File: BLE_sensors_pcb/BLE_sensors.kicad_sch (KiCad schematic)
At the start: 16 parts, among them J2 Conn_01x02, J3 USB_C_Receptacle, U1 BME280, U2 LSM303AHTR

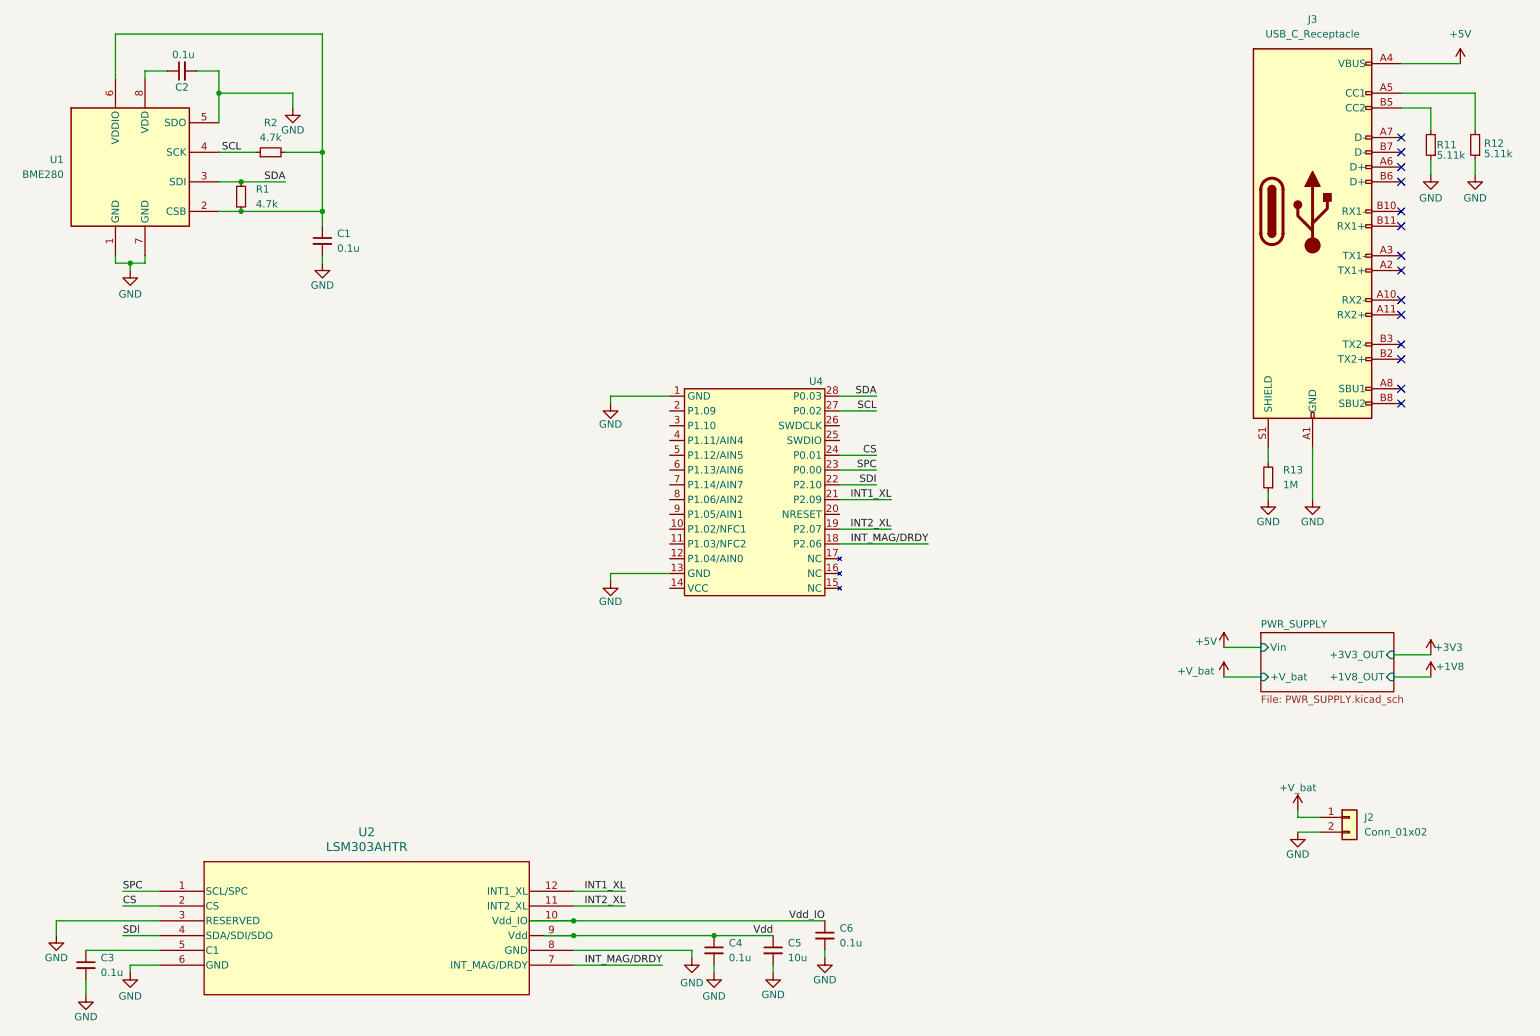
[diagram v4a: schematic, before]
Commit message: Added the usb to serial bridge
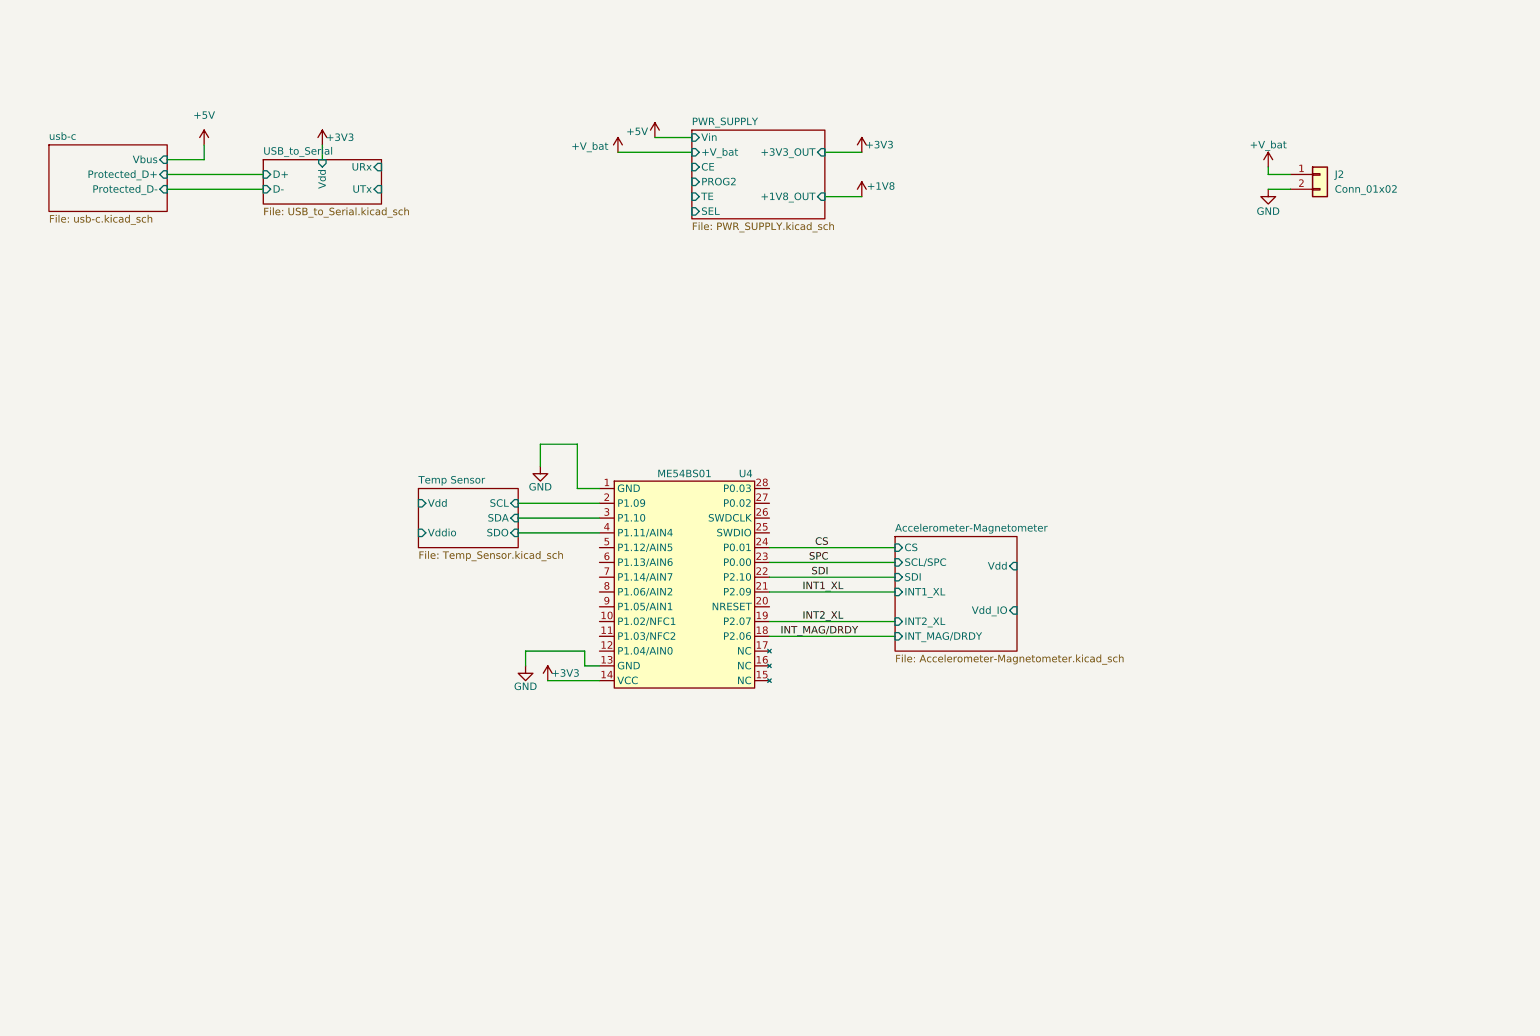
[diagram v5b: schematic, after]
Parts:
- removed C1, C2, C3, C4, C6: 0.1u, symbol Device:C_Small
- removed C5: 10u, symbol Device:C_Small
- removed J3: USB_C_Receptacle, symbol Connector:USB_C_Receptacle
- removed R1, R2: 4.7k, symbol Device:R_Small
- removed R11, R12: 5.11k, symbol Device:R_Small
- removed R13: 1M, symbol Device:R_Small
- removed U1: BME280, Package_LGA:Bosch_LGA-8_2.5x2.5mm_P0.65mm_ClockwisePinNumbering, symbol Sensor:BME280
- removed U2: LSM303AHTR, My_Libraries:LSM303AHTR, symbol My_Libraries:LSM303AHTR
- U4: value ~ -> ME54BS01
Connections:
- net +3V3: now also U4.14 (VCC)
- net Temp Sensor/SCL: now reaches U4.2 (P1.09)
- net Temp Sensor/SDA: now reaches U4.3 (P1.10)
- net Temp Sensor/SDO: now reaches U4.4 (P1.11/AIN4)
- net SCL: no longer names the net of U4.27 (P0.02)
- net SDA: no longer names the net of U4.28 (P0.03)
- no-connect marks 14 -> 0
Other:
- added sheet Accelerometer-Magnetometer (Accelerometer-Magnetometer.kicad_sch)
- added sheet Temp Sensor (Temp_Sensor.kicad_sch)
- added sheet USB_to_Serial (USB_to_Serial.kicad_sch)
- added sheet usb-c (usb-c.kicad_sch)
- sheet PWR_SUPPLY ports: added CE, PROG2, SEL, TE; removed none
- moved on the sheet: J2, U4

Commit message: Footprints and some pcb placement
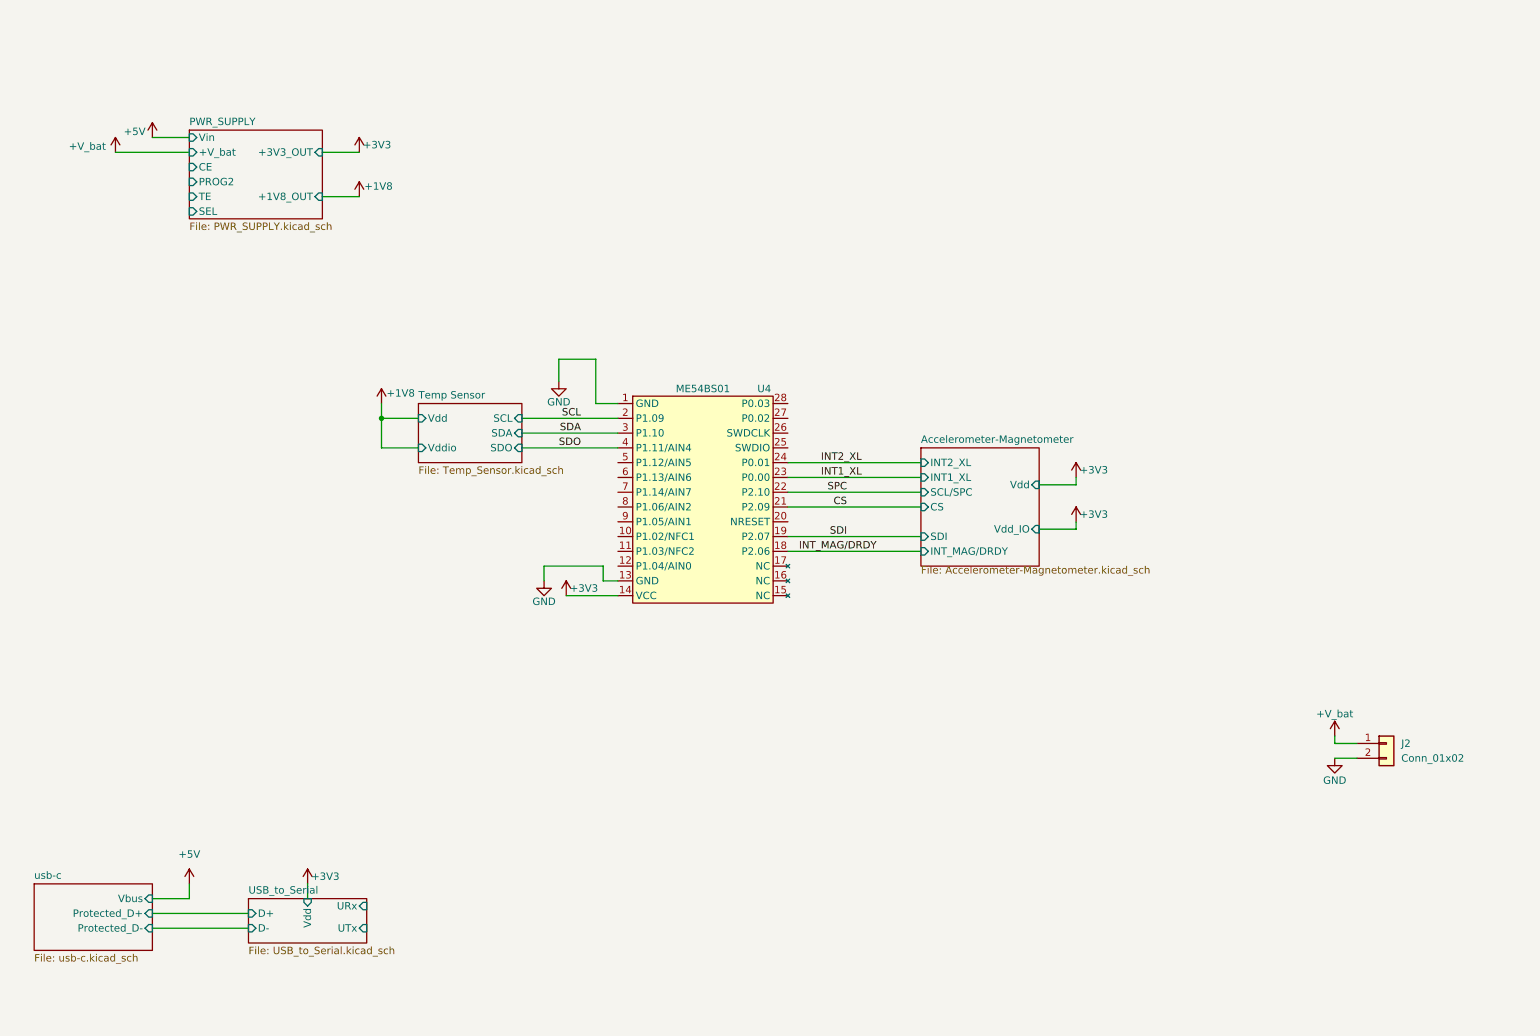
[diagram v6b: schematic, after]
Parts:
- J2: footprint (none) -> Connector_PinHeader_1.27mm:PinHeader_1x02_P1.27mm_Vertical
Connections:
- net CS: now also U4.21 (P2.09); no longer U4.24 (P0.01)
- net INT1_XL: now also U4.23 (P0.00); no longer U4.21 (P2.09)
- net INT2_XL: now also U4.24 (P0.01); no longer U4.19 (P2.07)
- net SDI: now also U4.19 (P2.07); no longer U4.22 (P2.10)
- net SPC: now also U4.22 (P2.10); no longer U4.23 (P0.00)
- net Temp Sensor/SCL renamed SCL
- net Temp Sensor/SDA renamed SDA
- net Temp Sensor/SDO renamed SDO
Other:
- moved on the sheet: J2, U4

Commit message: Initial pcb placement
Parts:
- added J1: Conn_ARM_SWD_TagConnect_TC2030-NL, Connector:Tag-Connect_TC2030-IDC-NL_2x03_P1.27mm_Vertical, symbol Connector:Conn_ARM_SWD_TagConnect_TC2030-NL
- added R10, R14: 100k, Resistor_SMD:R_0603_1608Metric, symbol Device:R_Small
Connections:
- net +3V3: now also J1.1 (VCC)
- net +V_bat: now also R10.1
- net GND: now also J1.5 (GND), R14.2
- net SCL: now also U4.3 (P1.10); no longer U4.2 (P1.09)
- net SDA: now also U4.2 (P1.09); no longer U4.3 (P1.10)
- net at U4.12 (P1.04/AIN0): now also R10.2, R14.1
- net nRESET: now reaches U4.20 (NRESET)
- net nRESET: now also J1.3 (~{RESET})
- net SWDIO: now reaches U4.25 (SWDIO)
- net SWDIO: now also J1.2 (SWDIO)
- net SWCLK: now reaches U4.26 (SWDCLK)
- net SWCLK: now also J1.4 (SWCLK)
- net SWO: now reaches U4.27 (P0.02)
- net SWO: now also J1.6 (SWO)
- net TX: now reaches U4.5 (P1.12/AIN5)
- net RX: now reaches U4.6 (P1.13/AIN6)
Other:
- sheet PWR_SUPPLY ports: added none; removed CE, PROG2, SEL, TE
- note added: "MAIN"
- moved on the sheet: J2, U4

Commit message: save
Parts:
- added R17: 10k, Resistor_SMD:R_0603_1608Metric, symbol Device:R_Small
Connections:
- net +3V3: now also R17.2
- net nRESET: now also R17.1
- no-connect marks 0 -> 6
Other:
- moved on the sheet: R10, R14, U4
